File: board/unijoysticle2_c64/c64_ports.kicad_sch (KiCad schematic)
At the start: 25 parts, among them J2 PORT JOY #1, J3 PORT JOY #2, SW3 MODE, SW4 SWAP, U4 74HC05, U5 74HC05, U6 74HC05

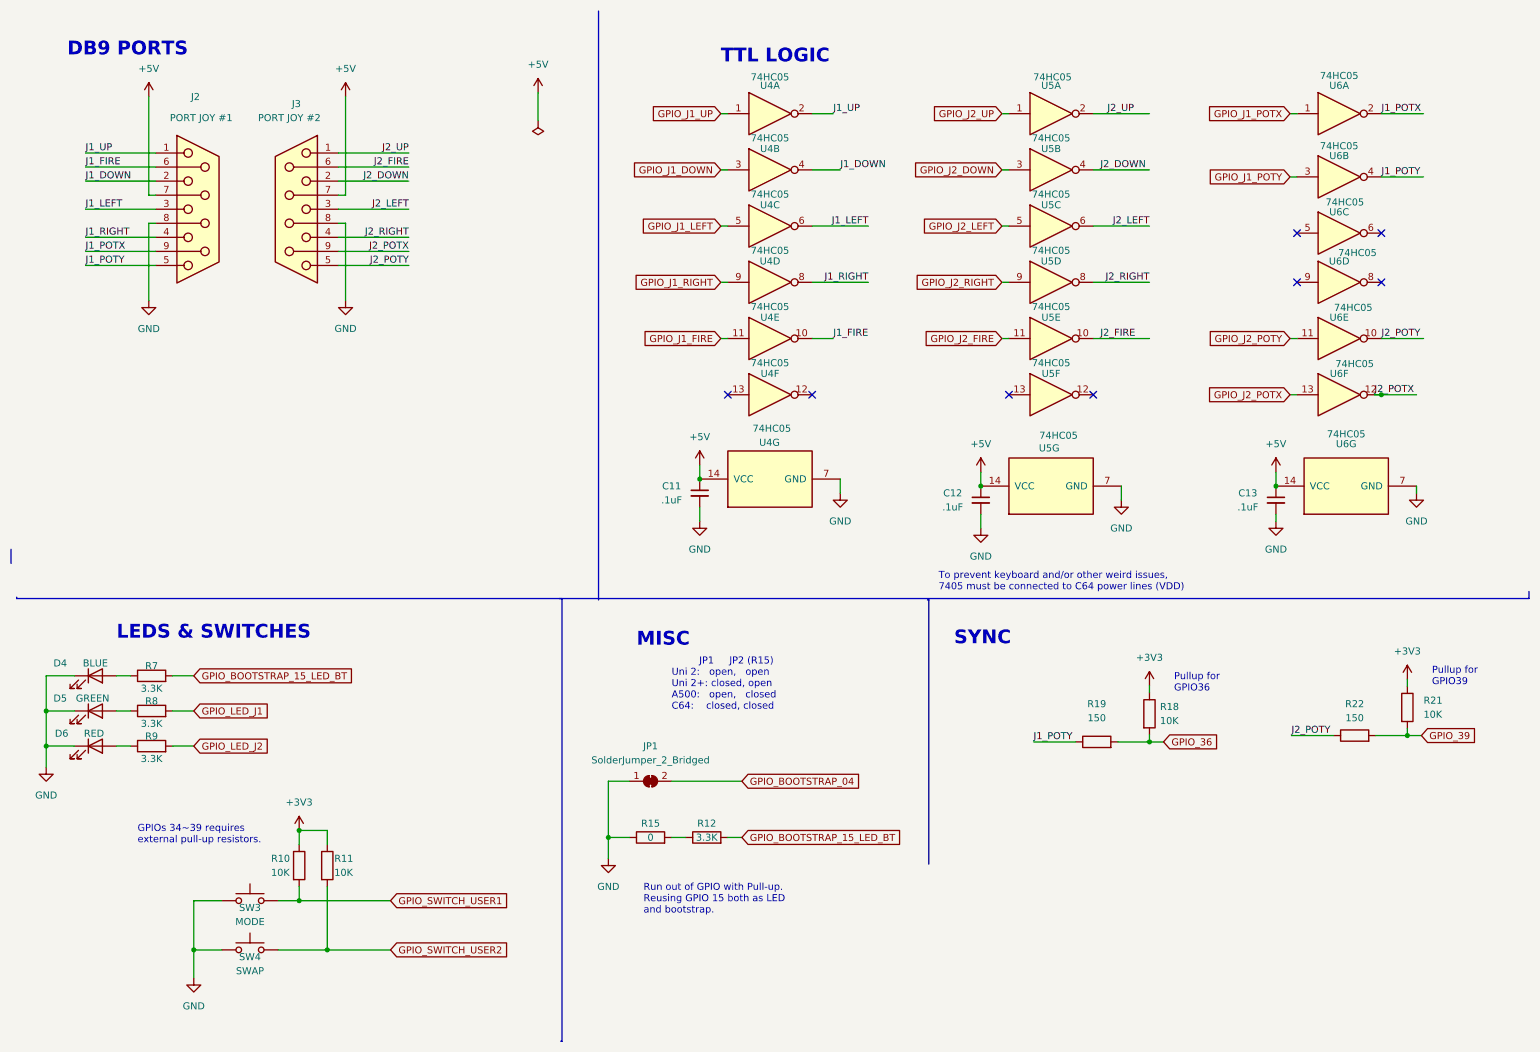
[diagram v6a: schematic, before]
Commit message: Unijoysticle C64 rev C
It is like A, with simplified sync circuit:
 - removed pull-down and pull-up resistor from SYNC

Seems to be working Ok.
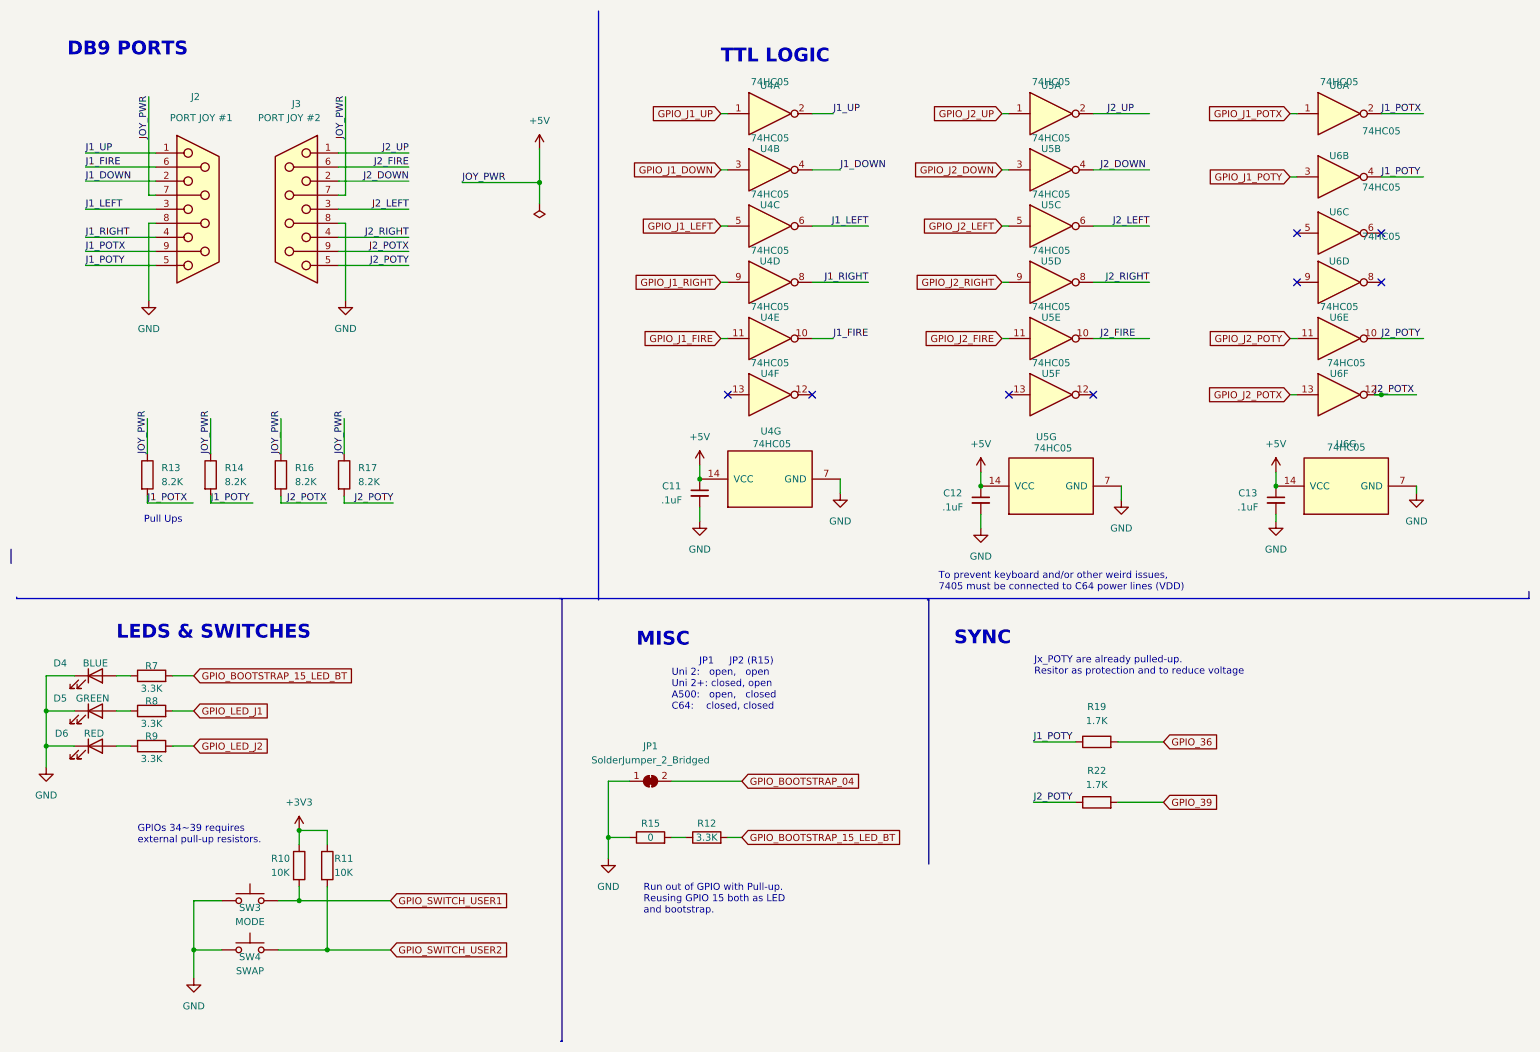
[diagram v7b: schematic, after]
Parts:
- removed R18, R21: 10K, Resistor_SMD:R_0805_2012Metric_Pad1.20x1.40mm_HandSolder, symbol Device:R
- added R13, R14, R16, R17: 8.2K, Resistor_SMD:R_0805_2012Metric_Pad1.20x1.40mm_HandSolder, symbol Device:R
- R19, R22: value 150 -> 1.7K
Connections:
- net +5V: now also R13.1, R14.1, R16.1, R17.1
- net J1_POTX: now also R13.2
- net J1_POTY: now also R14.2
- net J2_POTX: now also R16.2
- net J2_POTY: now also R17.2
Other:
- note added: "Jx_POTY are already pulled-up. Resitor as protection and to reduce voltage"
- note added: "Pull Ups"
- note removed: "Pullup for GPIO36"
- note removed: "Pullup for GPIO39"
- moved on the sheet: R22

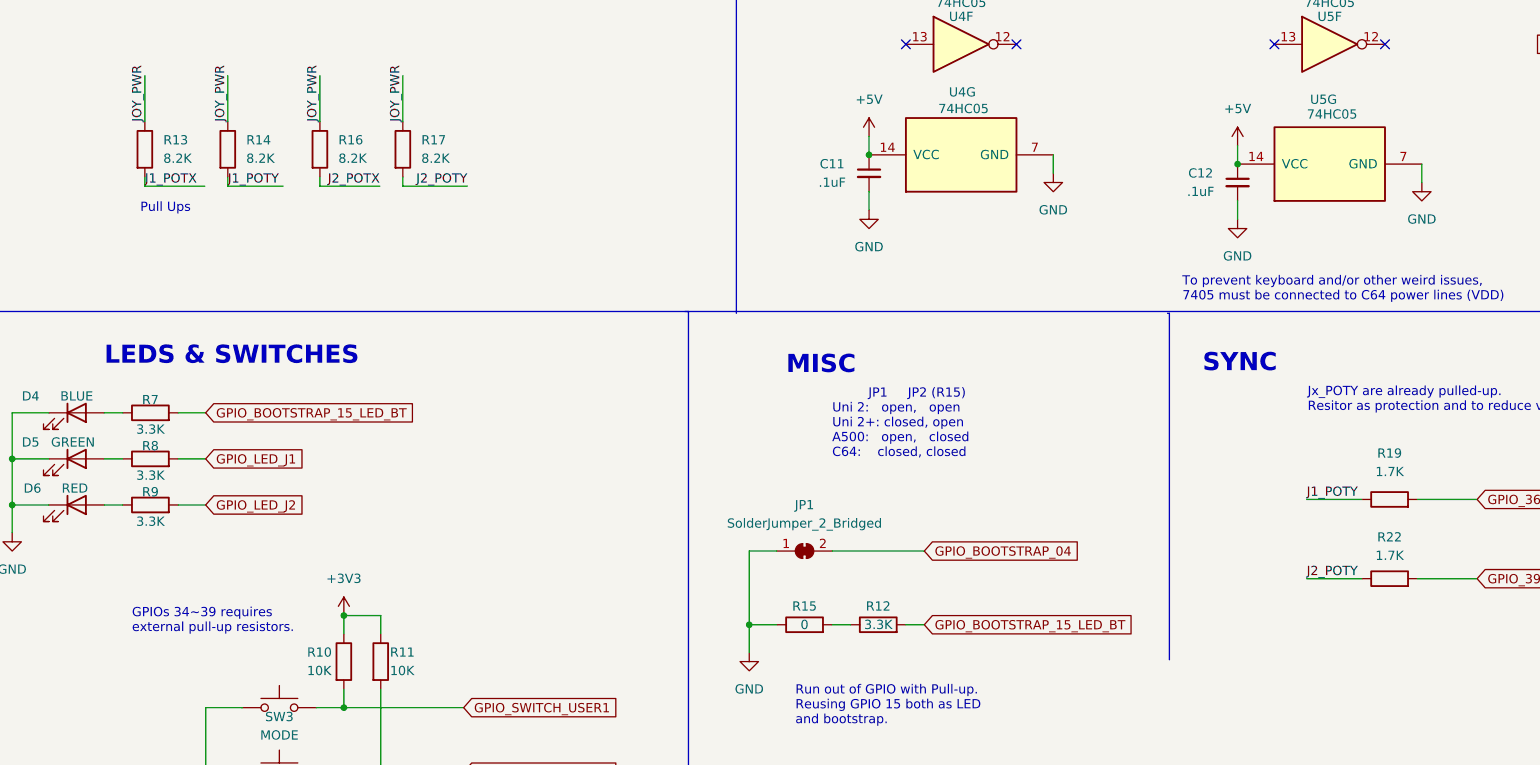
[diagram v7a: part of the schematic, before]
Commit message: C64: Update resistor values for Pull ups and SYNC
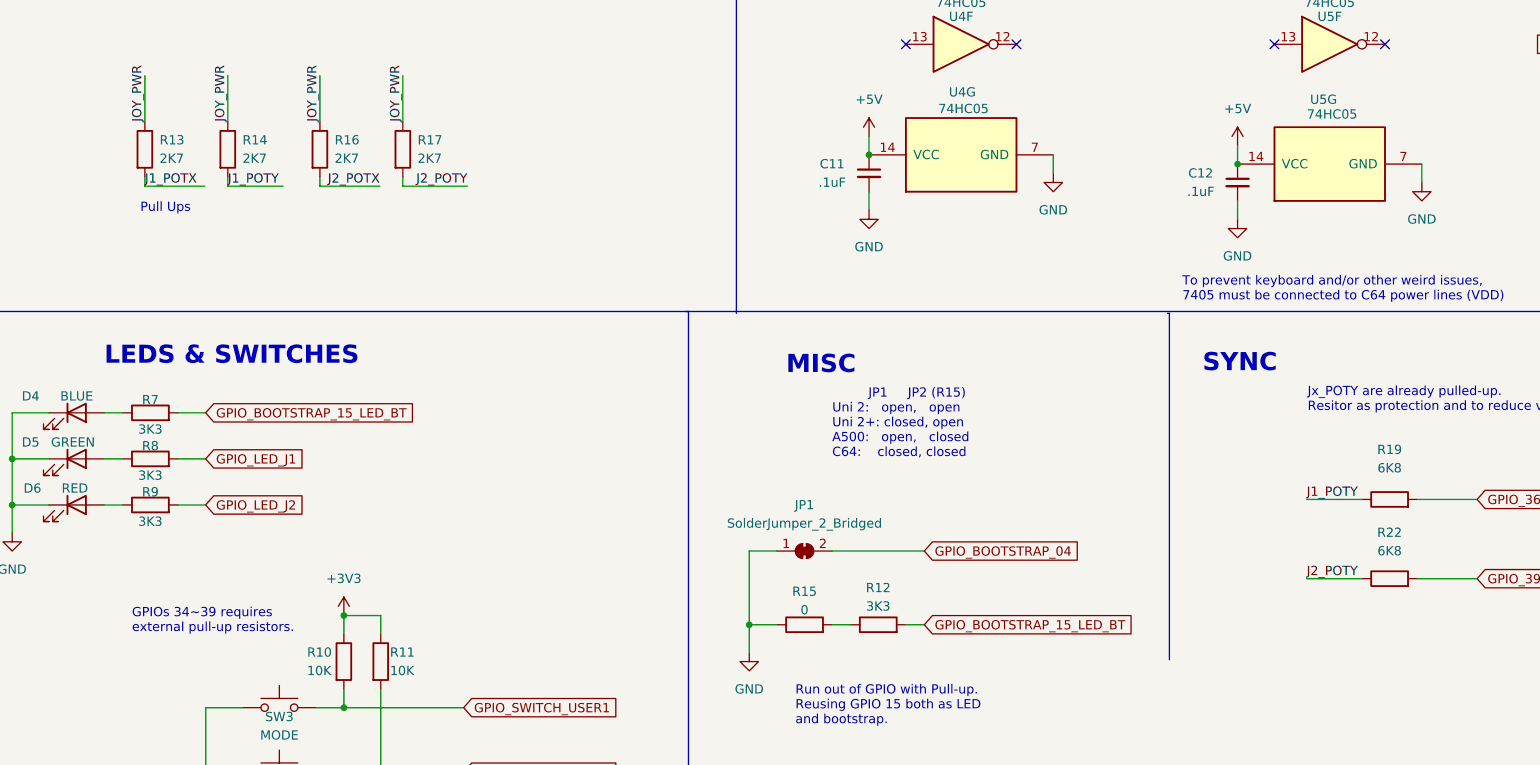
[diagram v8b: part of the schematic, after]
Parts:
- R12, R7, R8, R9: value 3.3K -> 3K3
- R13, R14, R16, R17: value 8.2K -> 2K7
- R19, R22: value 1.7K -> 6K8
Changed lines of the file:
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@@
     (in_bom yes) (on_board yes)
     (property "Reference" "R8" (id 0) (at 36.83 136.652 90))
-    (property "Value" "3.3K" (id 1) (at 36.83 140.716 90))
+    (property "Value" "3K3" (id 1) (at 36.83 140.716 90))
     (property "Footprint" "Resistor_SMD:R_0805_2012Metric_Pad1.20x1.40mm_HandSolder" (id 2) (at 36.83 140.208 90)
       (effects (font (size 1.27 1.27)) hide)
@@
     (in_bom yes) (on_board yes)
     (property "Reference" "R7" (id 0) (at 36.83 130.302 90))
-    (property "Value" "3.3K" (id 1) (at 36.83 134.366 90))
+    (property "Value" "3K3" (id 1) (at 36.83 134.366 90))
     (property "Footprint" "Resistor_SMD:R_0805_2012Metric_Pad1.20x1.40mm_HandSolder" (id 2) (at 36.83 133.858 90)
       (effects (font (size 1.27 1.27)) hide)
@@
     (in_bom yes) (on_board yes)
     (property "Reference" "R9" (id 0) (at 36.83 143.002 90))
-    (property "Value" "3.3K" (id 1) (at 36.83 147.066 90))
+    (property "Value" "3K3" (id 1) (at 36.83 147.066 90))
     (property "Footprint" "Resistor_SMD:R_0805_2012Metric_Pad1.20x1.40mm_HandSolder" (id 2) (at 36.83 146.558 90)
       (effects (font (size 1.27 1.27)) hide)
@@
   (symbol (lib_id "Device:R") (at 36.068 95.758 0) (unit 1)
     (in_bom yes) (on_board yes) (fields_autoplaced)
-    (property "Reference" "R13" (id 0) (at 38.608 94.4879 0)
-      (effects (font (size 1.27 1.27)) (justify left))
-    )
-    (property "Value" "8.2K" (id 1) (at 38.608 97.0279 0)
+    (property "Reference" "R13" (id 0) (at 38.1 94.4879 0)
+      (effects (font (size 1.27 1.27)) (justify left))
+    )
+    (property "Value" "2K7" (id 1) (at 38.1 97.0279 0)
       (effects (font (size 1.27 1.27)) (justify left))
     )
@@
   (symbol (lib_id "Device:R") (at 71.628 95.758 0) (unit 1)
     (in_bom yes) (on_board yes) (fields_autoplaced)
-    (property "Reference" "R17" (id 0) (at 74.168 94.4879 0)
-      (effects (font (size 1.27 1.27)) (justify left))
-    )
-    (property "Value" "8.2K" (id 1) (at 74.168 97.0279 0)
+    (property "Reference" "R17" (id 0) (at 73.66 94.4879 0)
+      (effects (font (size 1.27 1.27)) (justify left))
+    )
+    (property "Value" "2K7" (id 1) (at 73.66 97.0279 0)
       (effects (font (size 1.27 1.27)) (justify left))
     )
@@
   (symbol (lib_id "Device:R") (at 127 161.29 90) (unit 1)
     (in_bom yes) (on_board yes)
-    (property "Reference" "R15" (id 0) (at 127 158.75 90))
-    (property "Value" "0" (id 1) (at 127 161.29 90))
+    (property "Reference" "R15" (id 0) (at 127 156.718 90))
+    (property "Value" "0" (id 1) (at 127 159.258 90))
     (property "Footprint" "Resistor_SMD:R_0805_2012Metric_Pad1.20x1.40mm_HandSolder" (id 2) (at 127 163.068 90)
       (effects (font (size 1.27 1.27)) hide)
@@
   (symbol (lib_id "Device:R") (at 207.645 154.94 90) (unit 1)
     (in_bom yes) (on_board yes) (fields_autoplaced)
-    (property "Reference" "R22" (id 0) (at 207.645 149.225 90))
-    (property "Value" "1.7K" (id 1) (at 207.645 151.765 90))
+    (property "Reference" "R22" (id 0) (at 207.645 148.59 90))
+    (property "Value" "6K8" (id 1) (at 207.645 151.13 90))
     (property "Footprint" "Resistor_SMD:R_0805_2012Metric_Pad1.20x1.40mm_HandSolder" (id 2) (at 207.645 156.718 90)
       (effects (font (size 1.27 1.27)) hide)
@@
   (symbol (lib_id "Device:R") (at 207.645 144.018 90) (unit 1)
     (in_bom yes) (on_board yes) (fields_autoplaced)
-    (property "Reference" "R19" (id 0) (at 207.645 137.668 90))
-    (property "Value" "1.7K" (id 1) (at 207.645 140.208 90))
+    (property "Reference" "R19" (id 0) (at 207.645 137.16 90))
+    (property "Value" "6K8" (id 1) (at 207.645 139.7 90))
     (property "Footprint" "Resistor_SMD:R_0805_2012Metric_Pad1.20x1.40mm_HandSolder" (id 2) (at 207.645 145.796 90)
       (effects (font (size 1.27 1.27)) hide)
@@
   (symbol (lib_id "Device:R") (at 60.198 95.758 0) (unit 1)
     (in_bom yes) (on_board yes) (fields_autoplaced)
-    (property "Reference" "R16" (id 0) (at 62.738 94.4879 0)
-      (effects (font (size 1.27 1.27)) (justify left))
-    )
-    (property "Value" "8.2K" (id 1) (at 62.738 97.0279 0)
+    (property "Reference" "R16" (id 0) (at 62.23 94.4879 0)
+      (effects (font (size 1.27 1.27)) (justify left))
+    )
+    (property "Value" "2K7" (id 1) (at 62.23 97.0279 0)
       (effects (font (size 1.27 1.27)) (justify left))
     )
@@
   (symbol (lib_id "Device:R") (at 137.16 161.29 90) (unit 1)
     (in_bom yes) (on_board yes)
-    (property "Reference" "R12" (id 0) (at 137.16 158.75 90))
-    (property "Value" "3.3K" (id 1) (at 137.16 161.29 90))
+    (property "Reference" "R12" (id 0) (at 137.16 156.21 90))
+    (property "Value" "3K3" (id 1) (at 137.16 158.75 90))
     (property "Footprint" "Resistor_SMD:R_0805_2012Metric_Pad1.20x1.40mm_HandSolder" (id 2) (at 137.16 163.068 90)
       (effects (font (size 1.27 1.27)) hide)
@@
   (symbol (lib_id "Device:R") (at 47.498 95.758 0) (unit 1)
     (in_bom yes) (on_board yes) (fields_autoplaced)
-    (property "Reference" "R14" (id 0) (at 50.038 94.4879 0)
-      (effects (font (size 1.27 1.27)) (justify left))
-    )
-    (property "Value" "8.2K" (id 1) (at 50.038 97.0279 0)
-      (effects (font (size 1.27 1.27)) (justify left))
-    )
+    (property "Reference" "R14" (id 0) (at 49.53 94.4879 0)
+      (effects (font (size 1.27 1.27)) (justify left))
+    )
+    (property "Value" "2K7" (id 1) (at 49.53 97.0279 0)
+      (effects (font (size 1.27 1.27)) (justify left))
+    )
